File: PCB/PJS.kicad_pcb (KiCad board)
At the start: 2 copper layers, 127 x 127 mm, 40 parts, among them J1 HFW8R-1STE1H1LF_FFC, J10 SM02B-PASS-TBT_SwitchConnector, J2 SM02B-PASS-TBT_Connector, J3 SM02B-PASS-TBT_Connector, J4 SM02B-PASS-TBT_Connector, J5 SM02B-PASS-TBT_Connector, J6 SM02B-PASS-TBT_SwitchConnector, J7 SM02B-PASS-TBT_SwitchConnector, J8 SM02B-PASS-TBT_SwitchConnector, J9 SM02B-PASS-TBT_SwitchConnector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

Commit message: Schematic and PCB
First version with traces.
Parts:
- moved J6 47.2 mm to (180.9, 122.0)
- moved J10 47.2 mm to (181.0, 74.8)
- moved J7 23.6 mm to (181.0, 110.2)
- moved J9 23.6 mm to (181.0, 86.6)
- moved C8 17.2 mm to (96.3, 104.4), turned to 180 degrees
- moved C1 17.1 mm to (96.4, 60.6), turned to 90 degrees
- moved C2 17.0 mm to (96.3, 73.8), turned to 90 degrees
- moved C3 17.0 mm to (96.3, 87.1), turned to 90 degrees
- moved C7 17.0 mm to (96.3, 90.9), turned to 180 degrees
- moved C6 16.9 mm to (96.3, 77.7), turned to 180 degrees
- moved C4 16.8 mm to (96.3, 100.5), turned to 90 degrees
- moved C5 16.6 mm to (96.4, 64.3), turned to 180 degrees
- moved X4 9.66 mm to (124.3, 46.1), turned to 180 degrees
- moved A6 7.92 mm to (131.4, 131.2)
- moved R2 6.43 mm to (106.7, 76.6), turned to 90 degrees
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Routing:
- net /UAS_DriverIN2: track 0.00 -> 54.2 mm
- net /UAS_DriverIN1: track 0.00 -> 53.8 mm
- net /3.3V_Coin: track 0.00 -> 53.7 mm
- net /Door_RelayOut2: track 0.00 -> 53.3 mm
- net /LockA_DriverIN2: track 0.00 -> 50.5 mm
- net /LockA_DriverIN1: track 0.00 -> 50.1 mm
- net /Link_DriverIN2: track 0.00 -> 47.7 mm
- net /Link_DriverIN1: track 0.00 -> 47.2 mm
- net /S3_UAS: track 0.00 -> 36.6 mm
- net /S2_Door: track 0.00 -> 33.4 mm
- net /S1_Link: track 0.00 -> 27.5 mm
- net Net-(X3-Pad1): track 0.00 -> 11.8 mm
- net +12V: track 0.00 -> 11.6 mm, vias 0 -> 5
- net Net-(D1-Pad2): track 0.00 -> 11.1 mm
- net /UAS_DriverOUT1: track 0.00 -> 10.9 mm
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
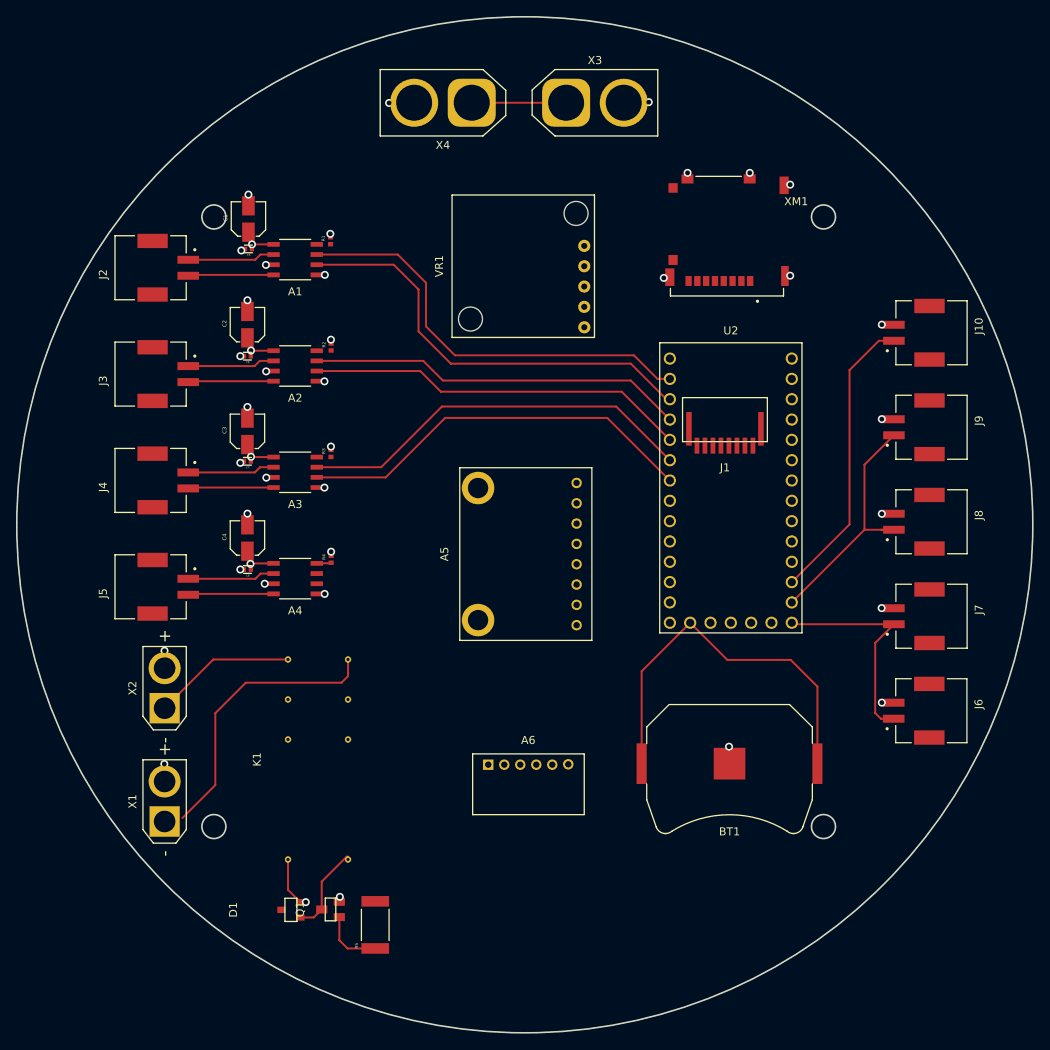
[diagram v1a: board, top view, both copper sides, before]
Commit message: PCB with TBS RF Receiver
All traces are connected. Planes and layers are not defined
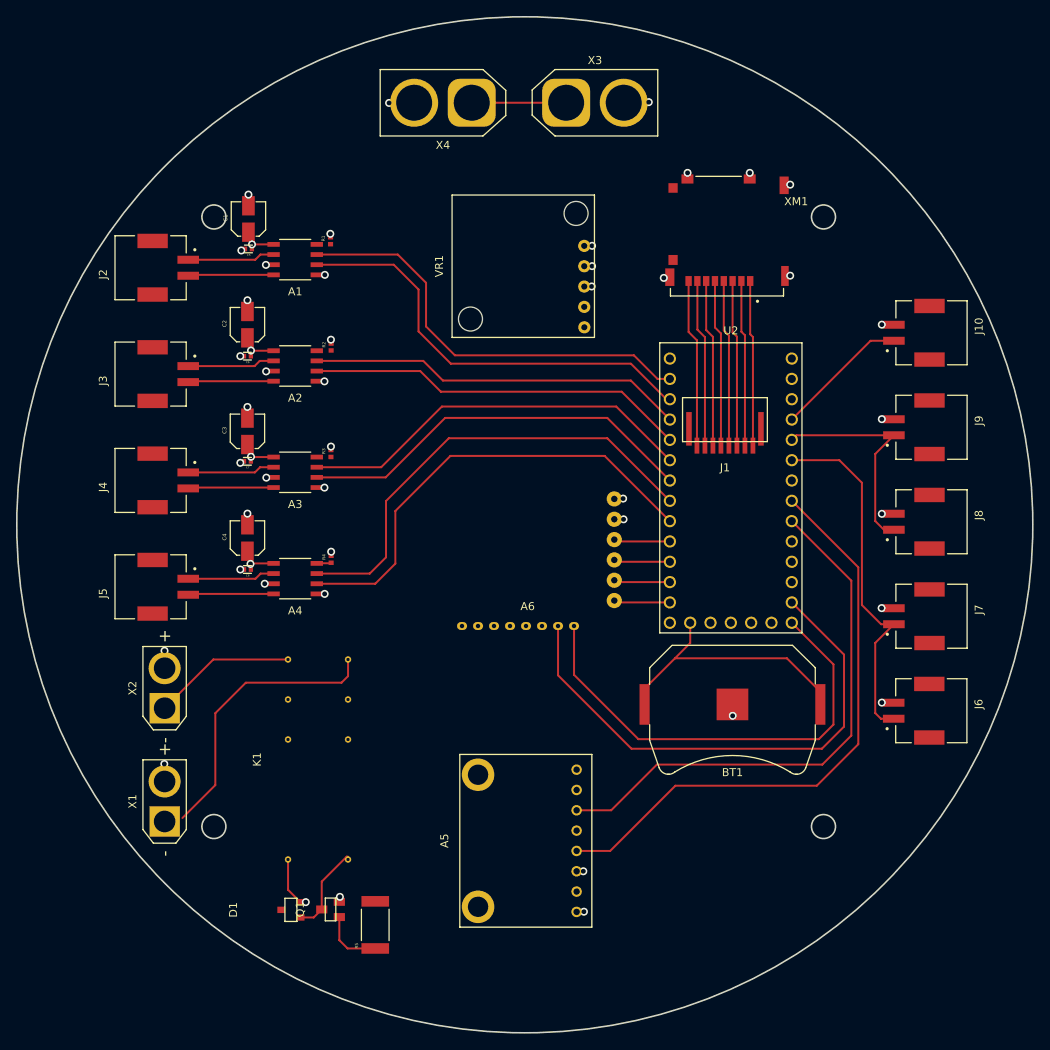
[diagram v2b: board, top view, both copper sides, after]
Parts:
- moved A5 35.8 mm to (131.1, 138.3)
- moved A6 27.7 mm to (131.3, 103.5), turned to 180 degrees
- moved BT1 7.41 mm to (156.9, 121.3)
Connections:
- J1 pad 1: /SD_DAT2 -> Net-(J1-Pad1)
- J1 pad 2: /SD_DAT3 -> Net-(J1-Pad2)
- J1 pad 3: /SD_CMD -> Net-(J1-Pad3)
- J1 pad 4: /SD_VDD -> Net-(J1-Pad4)
- J1 pad 5: /SD_CLK -> Net-(J1-Pad5)
- J1 pad 6: GND -> Net-(J1-Pad6)
- J1 pad 7: /SD_DAT0 -> Net-(J1-Pad7)
- J1 pad 8: /SD_DAT1 -> Net-(J1-Pad8)
- U2 pad 13: /S1_Link -> /RF_CH5
- U2 pad 14: /S2_Door -> /RF_CH6
- U2 pad 15: /S3_UAS -> Net-(U2-Pad15)
- U2 pad 21: Net-(U2-Pad21) -> /S1_Link
- U2 pad 22: Net-(U2-Pad22) -> /S2_Door
- U2 pad 23: Net-(U2-Pad23) -> /S3_UAS
- XM1 pad 1: Net-(J1-Pad16) -> Net-(J1-Pad1)
- XM1 pad 2: Net-(J1-Pad15) -> Net-(J1-Pad2)
- XM1 pad 3: Net-(J1-Pad14) -> Net-(J1-Pad3)
- XM1 pad 4: Net-(J1-Pad13) -> Net-(J1-Pad4)
- XM1 pad 5: Net-(J1-Pad12) -> Net-(J1-Pad5)
- XM1 pad 6: Net-(J1-Pad11) -> Net-(J1-Pad6)
- XM1 pad 7: Net-(J1-Pad10) -> Net-(J1-Pad7)
- XM1 pad 8: Net-(J1-Pad9) -> Net-(J1-Pad8)
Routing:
- net /Alt_SCK: track 0.00 -> 74.6 mm
- net /Alt_SDI: track 0.00 -> 68.1 mm
- net /RF_CH6: track 0.00 -> 65.1 mm
- net /LockB_DriverIN1: track 0.00 -> 58.5 mm
- net /LockB_DriverIN2: track 0.00 -> 58.0 mm
- net /RF_CH5: track 0.00 -> 57.8 mm
- net Net-(J1-Pad8): track 0.00 -> 21.0 mm
- net Net-(J1-Pad7): track 0.00 -> 21.0 mm
- net Net-(J1-Pad6): track 0.00 -> 20.9 mm
- net Net-(J1-Pad5): track 0.00 -> 20.9 mm
- net Net-(J1-Pad4): track 0.00 -> 20.8 mm
- net Net-(J1-Pad3): track 0.00 -> 20.8 mm
- net Net-(J1-Pad2): track 0.00 -> 20.8 mm
- net Net-(J1-Pad1): track 0.00 -> 20.7 mm
- net /S3_UAS: track 36.6 -> 16.8 mm
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
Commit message: almost all 3d models
a few minor bugs fixed, but traces should be redone after CDR and the bugs are mostly to do with weird footprint things
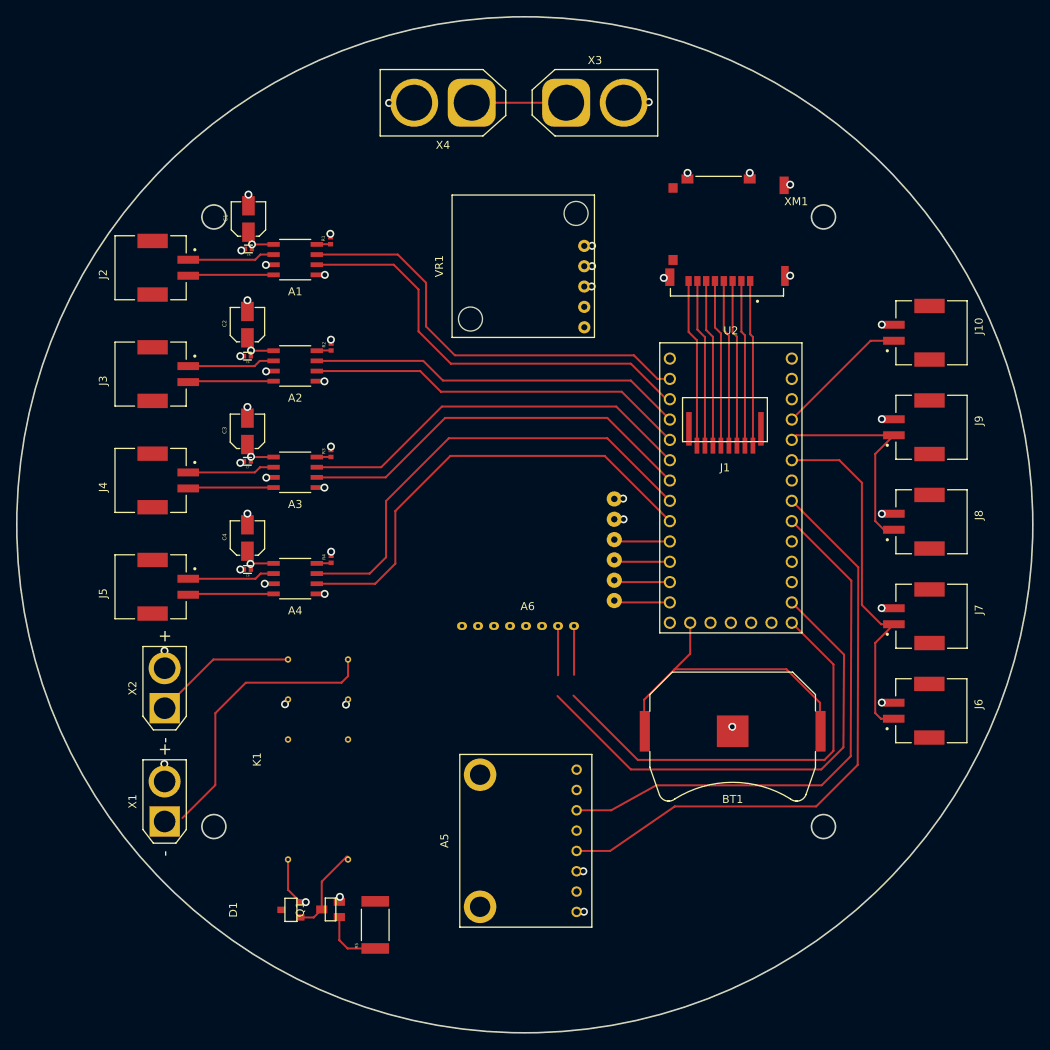
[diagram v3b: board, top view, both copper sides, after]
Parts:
- moved BT1 3.35 mm to (156.9, 124.6)
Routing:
- net /RF_CH5: track 57.8 -> 60.9 mm
- net /RF_CH6: track 65.1 -> 67.7 mm
- net Net-(A2-Pad4): track 0.00 -> 1.81 mm
- net Net-(A3-Pad4): track 0.00 -> 1.78 mm
- net Net-(A1-Pad4): track 0.00 -> 1.73 mm
- net /3.3V_Coin: track 34.1 -> 35.5 mm
- net /Alt_SDI: track 68.1 -> 69.0 mm
- net /Alt_SCK: track 74.6 -> 75.5 mm
- net +12V: vias 6 -> 8

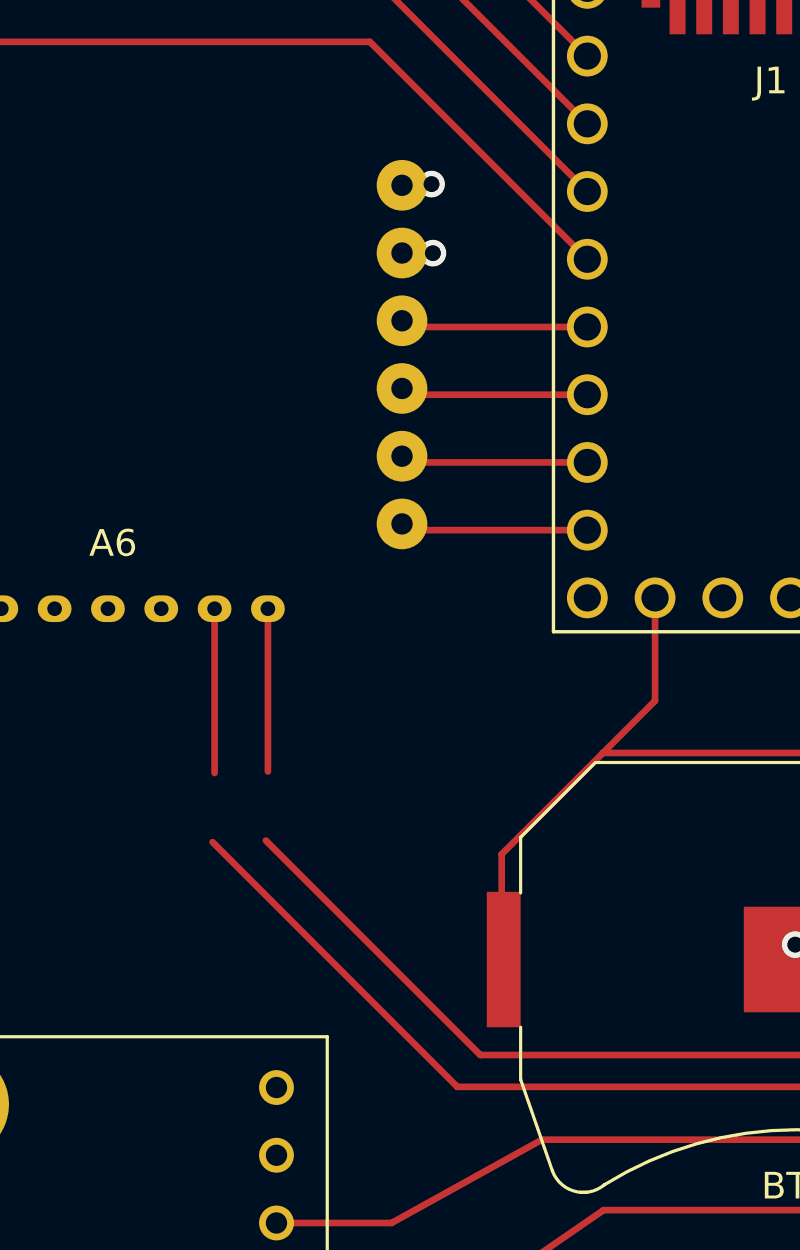
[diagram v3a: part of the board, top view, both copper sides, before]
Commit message: Receiver fix and drv resistor fix
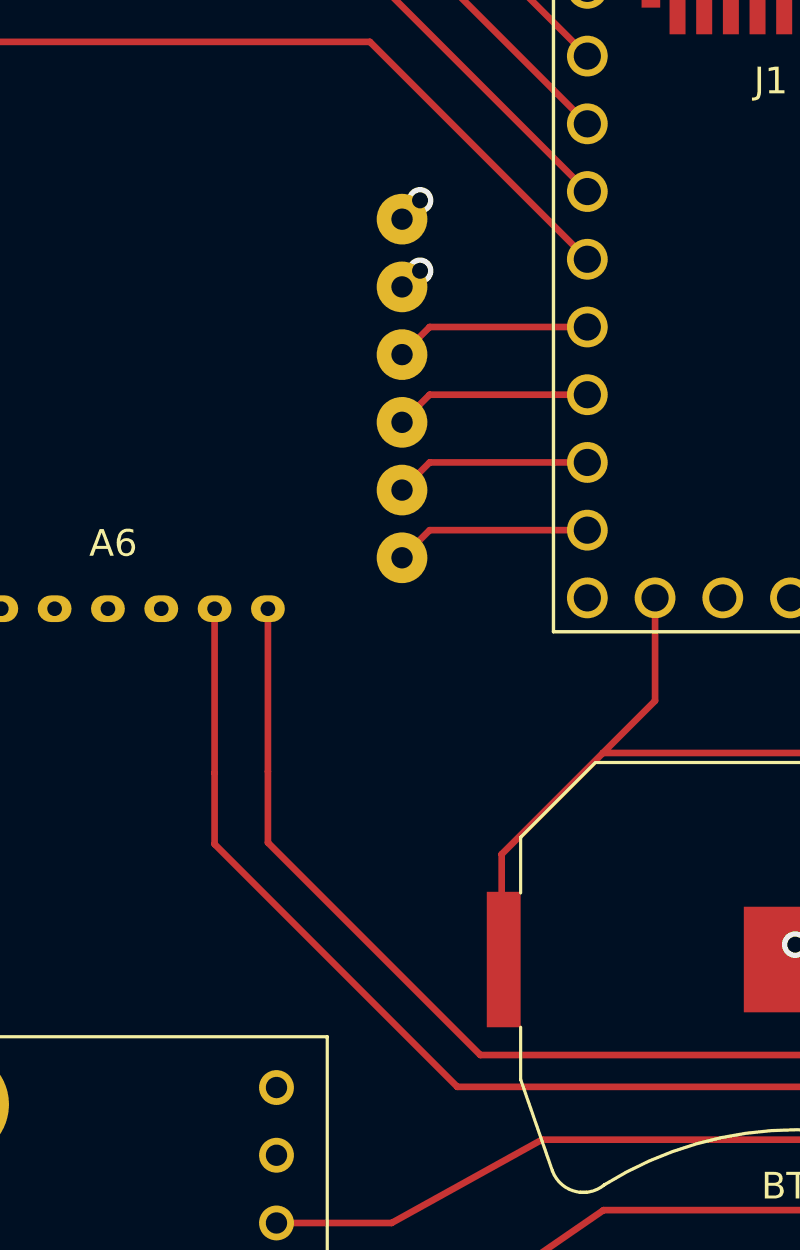
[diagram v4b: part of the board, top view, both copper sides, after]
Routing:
- net /RF_CH5: track 60.9 -> 63.4 mm
- net /RF_CH6: track 67.7 -> 70.2 mm
